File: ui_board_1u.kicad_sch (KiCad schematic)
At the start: 39 parts, among them J1 X9555WV-2x06-6TV01, U1 AFC01-S30FCA-00, U2 SPX3819M5-L, U3 TPS61040DBV

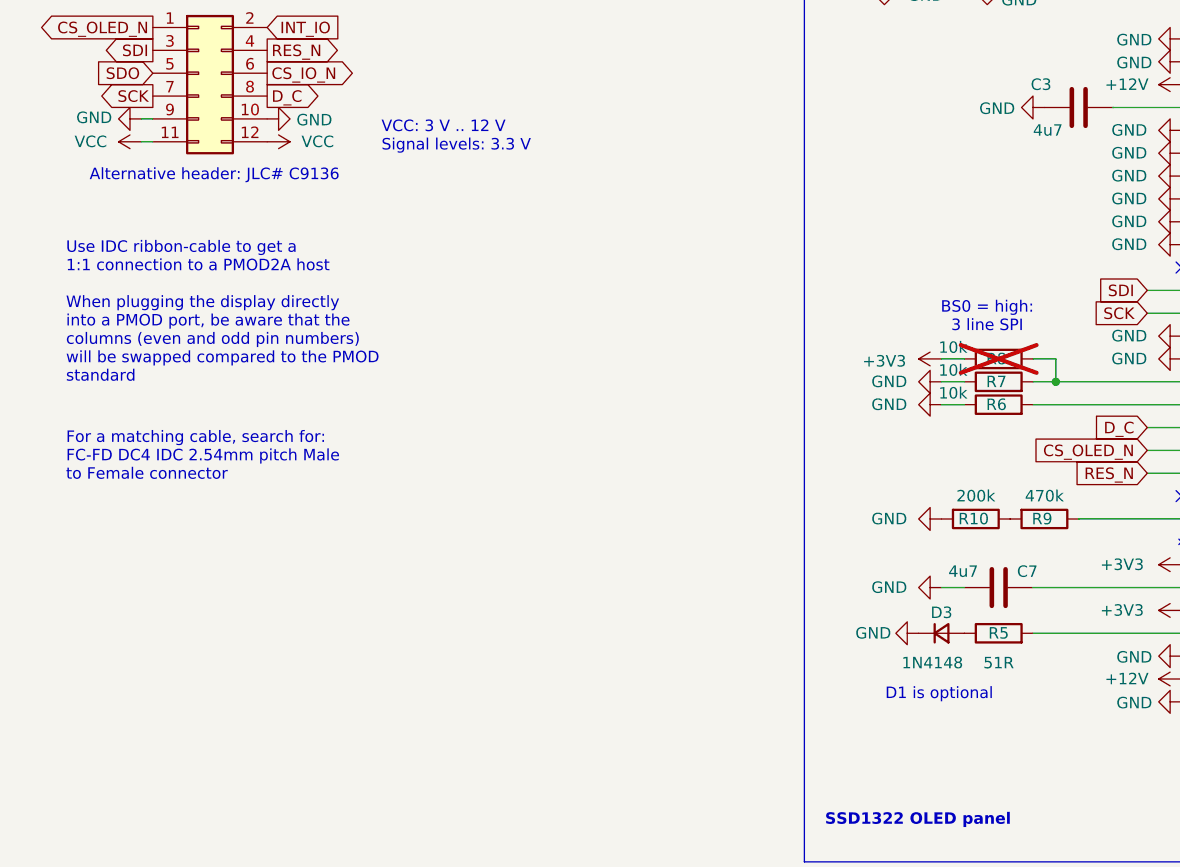
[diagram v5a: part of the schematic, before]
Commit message: fix some more typos in the schematic
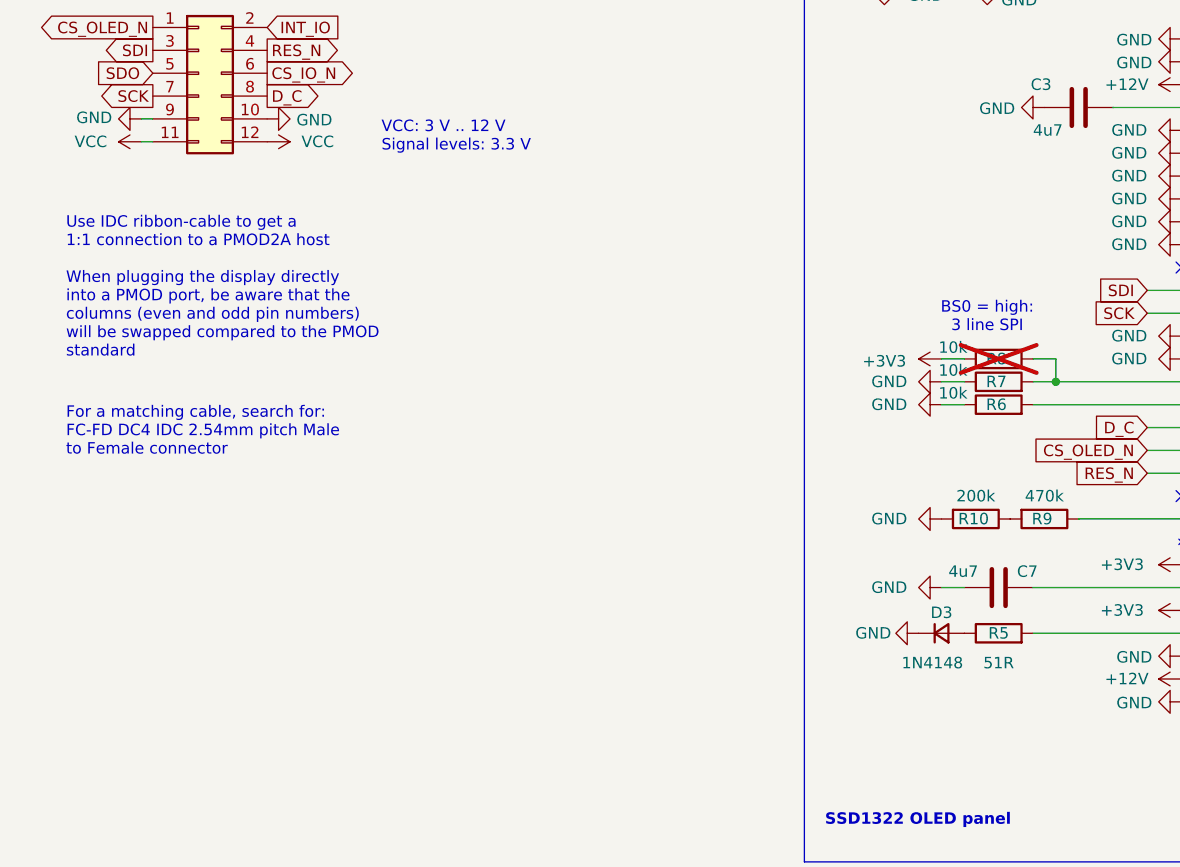
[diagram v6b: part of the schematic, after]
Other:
- note removed: "Alternative header: JLC# C9136"
- note removed: "D1 is optional"
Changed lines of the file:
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@@
-		)
-	)
-	(text "Alternative header: JLC# C9136"
-		(exclude_from_sim no)
-		(at 51.308 69.85 0)
-		(effects
-			(font
-				(size 1.27 1.27)
-			)
 		)
 	)
@@
 	(text "Use IDC ribbon-cable to get a \n1:1 connection to a PMOD2A host\n\nWhen plugging the display directly\ninto a PMOD port, be aware that the\ncolumns (even and odd pin numbers)\nwill be swapped compared to the PMOD\nstandard\n\n"
 		(exclude_from_sim no)
-		(at 34.798 86.106 0)
+		(at 34.798 83.312 0)
 		(effects
 			(font
@@
 	(text "For a matching cable, search for:\nFC-FD DC4 IDC 2.54mm pitch Male \nto Female connector "
 		(exclude_from_sim no)
-		(at 34.798 101.092 0)
+		(at 34.798 98.298 0)
 		(effects
 			(font
@@
 		(exclude_from_sim no)
 		(at 223.774 102.616 0)
-		(effects
-			(font
-				(size 1.27 1.27)
-			)
-		)
-	)
-	(text "D1 is optional"
-		(exclude_from_sim no)
-		(at 131.826 127.508 0)
 		(effects
 			(font
@@
 			"AAAAAAAAAAAAAAAAAAAAAAAAAAAAAAAAAAAAAAAAAAAAAAAAAAAAAAAAAAAAAAAAAAAAAAAAAAAA"
 			"AAAAAAAAAAAAAAAAAAAAAAAAAAAAAAAAAAAAAAAAAAAAAAAAAAAAAAAAAAAAAAAAAAAAAAAAAAAA"
+			"AAAAAAAAAAAAAAAAAAAAAAAAAAAAAAAAAAAAAAAAAAAAAAAAAAAAAAAAAAAAAAAAAAAAAAAAAAAA"
+			"AAAAAAAAAAAAAAAAAAAAAAAAAAAAAAAAAAAAAAAAAAAAAAAAAAAAAAAAAAAAAAAAAAAAAAAAAAAA"
+			"AAAAAAAAAAAAAAAAAAAAAAAAAAAAAAAAAAAAAAAAAAAAAAAAAAAAAAAAAAAAAAAAAAAAAAAAAAAA"
+			"AAAAAAAAAAAAAAAAAAAAAAAAAAAAAAAAAAAAAAAAAAAAAAAAAAAAAAAAAAAAAAAAAAAAAAAAAAAA"
+			"AAAAAAAAAAAAAAAAAAAAAAAAAAAAAAAAAAAAAAAAAAAAAAAAAAAAAAAAAAAAAAAAAAAAAAAAAAAA"
+			"AAAAAAAAAAAAAAAAAAAAAAAAAAAAAAAAAAAAAAAAAAAAAAAAAAAAAAAAAAAAAAAAAAAAAAAAAAAA"
+			"AAAAAAAAAAAAAAAAAAAAAAAAAAAAAAAAAAAAAAAAAAAAAAAAAAAAAAAAAAAAAAAAAAAAAAAAAAAA"
+			"AAAAAAAAAAAAAAAAAAAAAAAAAAAAAAAAAAAAAAAAAAAAAAAAAAAAAAAAAAAAAAAAAAAAAAAAAAAA"
+			"AAAAAAAAAAAAAAAAAAAAAAAAAAAAAAAAAAAAAAAAAAAAAAAAAAAAAAAAAAAAAAAAAAAAAAAAAAAA"
+			"AAAAAAAAAAAAAAAAAAAAAAAAAAAAAAAAAAAAAAAAAAAAAAAAAAAAAAAAAAAAAAAAAAAAAAAAAAAA"
+			"AAAAAAAAAAAAAAAAAAAAAAAAAAAAAAAAAAAAAAAAAAAAAAAAAAAAAAAAAAAAAAAAAAAAAAAAAAAA"
+			"AAAAAAAAAAAAAAAAAAAAAAAAAAAAAAAAAAAAAAAAAAAAAAAAAAAAAAAAAAAAAAAAAAAAAAAAAAAA"
+			"AAAAAAAAAAAAAAAAAAAAAAAAAAAAAAAAAAAAAAAAAAAAAAAAAAAAAAAAAAAAAAAAAAAAAAAAAAAA"
+			"AAAAAAAAAAAAAAAAAAAAAAAAAAAAAAAAAAAAAAAAAAAAAAAAAAAAAAAAAAAAAAAAAAAAAAAAAAAA"
+			"AAAAAAAAAAAAAAAAAAAAAAAAAAAAAAAAAAAAAAAAAAAAAAAAAAAAAAAAAAAAAAAAAAAAAAAAAAAA"
+			"AAAAAAAAAAAAAAAAAAAAAAAAAAAAAAAAAAAAAAAAAAAAAAAAAAAAAAAAAAAAAAAAAAAAAAAAAAAA"
+			"AAAAAAAAAAAAAAAAAAAAAAAAAAAAAAAAAAAAAAAAAAAAAAAAAAAAAAAAAAAAAAAAAAAAAAAAAAAA"
+			"AAAAAAAAAAAAAAAAAAAAAAAAAAAAAAAAAAAAAAAAAAAAAAAAAAAAAAAAAAAAAAAAAAAAAAAAAAAA"
